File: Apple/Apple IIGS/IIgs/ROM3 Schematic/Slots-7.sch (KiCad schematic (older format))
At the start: 22 parts, among them J1 Apple_II_Slot, J2 Apple_II_Slot, J3 Apple_II_Slot, J4 Apple_II_Slot, J5 Apple_II_Slot, J6 Apple_II_Slot, J7 Apple_II_Slot

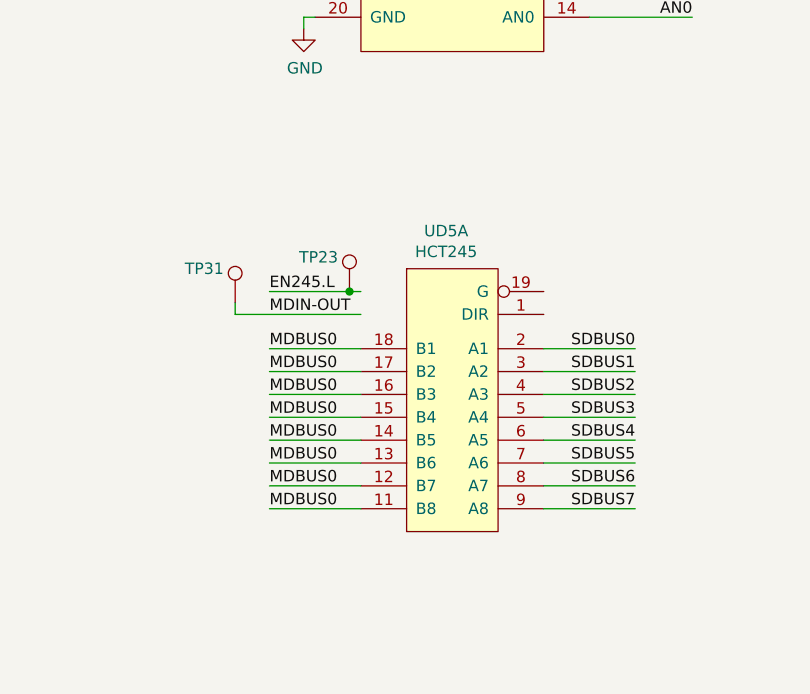
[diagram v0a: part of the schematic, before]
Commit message: Clean-up after detailed circuit analysis - Fixed Reference to library in project file - Fixed BABUS tags on HCT245 (had wrong nets) - Flipped HCT245 circuits on MEGAII page to better match In/Out flow - Changed HCT245 symbol to move enable and DIR to better match In/Out Flow - Changed HCT245 into multi-unit symbol to put VCC/GND pins on Unit B - Fixed MEGAII designator - Fixed ADBUS nets on HCT245 (should be ABUS!) - Added notes with lessons learned from circuit deep-dive
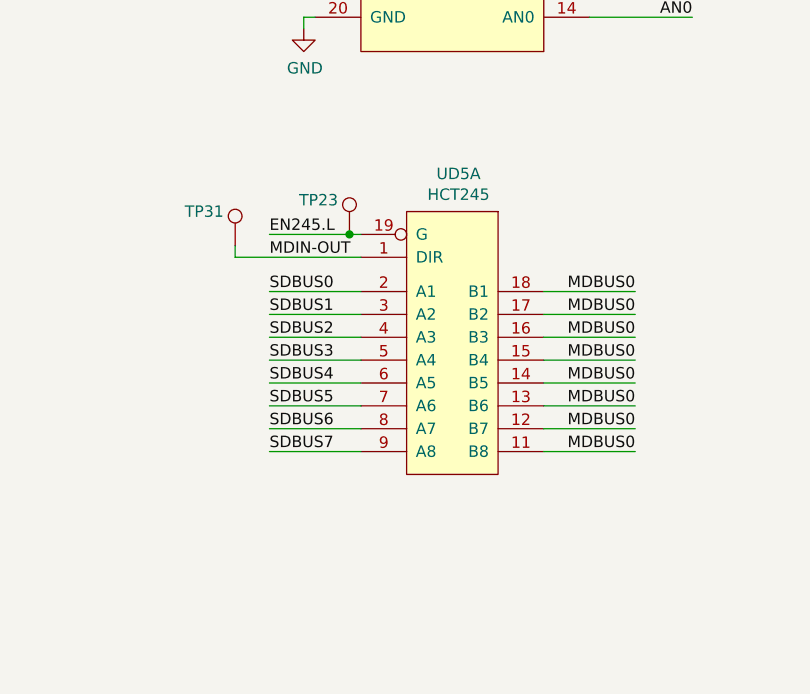
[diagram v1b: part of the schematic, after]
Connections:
- net EN245.L: now also UD5.19 (G)
- net MDIN-OUT: now also UD5.1 (DIR)
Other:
- moved on the sheet: TP23, TP31, UD5A
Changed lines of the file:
@@
-	1    0    0    -1
-$EndComp
-$Comp
-L IIgs-Schematic:HCT245 UD5
-U 1 1 5BF2195F
-P 2650 8500
-F 0 "UD5" H 2623 9265 50  0000 C CNN
-F 1 "HCT245" H 2623 9174 50  0000 C CNN
-F 2 "" H 2450 9150 50  0001 C CNN
-F 3 "" H 2450 9150 50  0001 C CNN
-	1    2650 8500
 	1    0    0    -1
 $EndComp
@@
 Wire Wire Line
 	2000 6800 2000 6850
-Wire Wire Line
-	3050 8250 3450 8250
-Text Label 3450 8250 2    50   ~ 0
-SDBUS0
-Wire Wire Line
-	3050 8350 3450 8350
-Text Label 3450 8350 2    50   ~ 0
-SDBUS1
-Wire Wire Line
-	3050 8450 3450 8450
-Text Label 3450 8450 2    50   ~ 0
-SDBUS2
-Wire Wire Line
-	3050 8550 3450 8550
-Text Label 3450 8550 2    50   ~ 0
-SDBUS3
-Wire Wire Line
-	3050 8650 3450 8650
-Text Label 3450 8650 2    50   ~ 0
-SDBUS4
-Wire Wire Line
-	3050 8750 3450 8750
-Text Label 3450 8750 2    50   ~ 0
-SDBUS5
-Wire Wire Line
-	3050 8850 3450 8850
-Text Label 3450 8850 2    50   ~ 0
-SDBUS6
-Wire Wire Line
-	3050 8950 3450 8950
-Text Label 3450 8950 2    50   ~ 0
-SDBUS7
-Text Label 1850 8250 0    50   ~ 0
+Text Label 3450 8000 2    50   ~ 0
 MDBUS0
-Text Label 1850 8350 0    50   ~ 0
+Text Label 3450 8100 2    50   ~ 0
 MDBUS0
-Text Label 1850 8450 0    50   ~ 0
+Text Label 3450 8200 2    50   ~ 0
 MDBUS0
-Text Label 1850 8550 0    50   ~ 0
+Text Label 3450 8300 2    50   ~ 0
 MDBUS0
-Text Label 1850 8650 0    50   ~ 0
+Text Label 3450 8400 2    50   ~ 0
 MDBUS0
-Text Label 1850 8750 0    50   ~ 0
+Text Label 3450 8500 2    50   ~ 0
 MDBUS0
-Text Label 1850 8850 0    50   ~ 0
+Text Label 3450 8600 2    50   ~ 0
 MDBUS0
-Text Label 1850 8950 0    50   ~ 0
+Text Label 3450 8700 2    50   ~ 0
 MDBUS0
-Wire Wire Line
-	1850 8850 2250 8850
-Wire Wire Line
-	2250 8750 1850 8750
-Wire Wire Line
-	1850 8650 2250 8650
-Wire Wire Line
-	2250 8550 1850 8550
-Wire Wire Line
-	1850 8450 2250 8450
-Wire Wire Line
-	1850 8350 2250 8350
-Wire Wire Line
-	2250 8250 1850 8250
-Text Label 1850 8100 0    50   ~ 0
+Text Label 1850 7850 0    50   ~ 0
 MDIN-OUT
 $Comp
 L Connector:TestPoint TP31
 U 1 1 5E2A0BC4
-P 1700 8050
-F 0 "TP31" H 1650 8200 50  0000 R CNN
-F 1 "TestPoint" H 1642 8168 50  0001 R CNN
-F 2 "" H 1900 8050 50  0001 C CNN
-F 3 "~" H 1900 8050 50  0001 C CNN
-	1    1700 8050
+P 1700 7800
+F 0 "TP31" H 1650 7950 50  0000 R CNN
+F 1 "TestPoint" H 1642 7918 50  0001 R CNN
+F 2 "" H 1900 7800 50  0001 C CNN
+F 3 "~" H 1900 7800 50  0001 C CNN
+	1    1700 7800
 	1    0    0    -1
 $EndComp
 Wire Wire Line
-	1700 8100 1700 8050
-Wire Wire Line
-	1700 8100 2250 8100
-Wire Wire Line
-	2250 8000 2200 8000
-Text Label 1850 8000 0    50   ~ 0
+	1700 7850 1700 7800
+Wire Wire Line
+	1700 7850 2250 7850
+Wire Wire Line
+	2250 7750 2200 7750
+Text Label 1850 7750 0    50   ~ 0
 EN245.L
 $Comp
 L Connector:TestPoint TP23
 U 1 1 5E36B3FB
-P 2200 8000
-F 0 "TP23" H 2150 8150 50  0000 R CNN
-F 1 "TestPoint" H 2142 8118 50  0001 R CNN
-F 2 "" H 2400 8000 50  0001 C CNN
-F 3 "~" H 2400 8000 50  0001 C CNN
-	1    2200 8000
+P 2200 7750
+F 0 "TP23" H 2150 7900 50  0000 R CNN
+F 1 "TestPoint" H 2142 7868 50  0001 R CNN
+F 2 "" H 2400 7750 50  0001 C CNN
+F 3 "~" H 2400 7750 50  0001 C CNN
+	1    2200 7750
 	1    0    0    -1
 $EndComp
-Connection ~ 2200 8000
-Wire Wire Line
-	2200 8000 1850 8000
-Wire Wire Line
-	1850 8950 2250 8950
+Connection ~ 2200 7750
+Wire Wire Line
+	2200 7750 1850 7750
 $Comp
 L Device:R_Small R113
@@
 Text Notes 2300 700  0    50   ~ 0
 Global labels not shown
+Wire Wire Line
+	3450 8700 3050 8700
+Wire Wire Line
+	3050 8000 3450 8000
+Wire Wire Line
+	3450 8100 3050 8100
+Wire Wire Line
+	3450 8200 3050 8200
+Wire Wire Line
+	3050 8300 3450 8300
+Wire Wire Line
+	3450 8400 3050 8400
+Wire Wire Line
+	3050 8500 3450 8500
+Wire Wire Line
+	3450 8600 3050 8600
+Text Label 1850 8700 0    50   ~ 0
+SDBUS7
+Wire Wire Line
+	2250 8700 1850 8700
+Text Label 1850 8600 0    50   ~ 0
+SDBUS6
+Wire Wire Line
+	2250 8600 1850 8600
+Text Label 1850 8500 0    50   ~ 0
+SDBUS5
+Wire Wire Line
+	2250 8500 1850 8500
+Text Label 1850 8400 0    50   ~ 0
+SDBUS4
+Wire Wire Line
+	2250 8400 1850 8400
+Text Label 1850 8300 0    50   ~ 0
+SDBUS3
+Wire Wire Line
+	2250 8300 1850 8300
+Text Label 1850 8200 0    50   ~ 0
+SDBUS2
+Wire Wire Line
+	2250 8200 1850 8200
+Text Label 1850 8100 0    50   ~ 0
+SDBUS1
+Wire Wire Line
+	2250 8100 1850 8100
+Text Label 1850 8000 0    50   ~ 0
+SDBUS0
+Wire Wire Line
+	2250 8000 1850 8000
+$Comp
+L IIgs-Schematic:HCT245 UD5
+U 1 1 5BF2195F
+P 2650 8250
+F 0 "UD5" H 2623 9015 50  0000 C CNN
+F 1 "HCT245" H 2623 8924 50  0000 C CNN
+F 2 "" H 2450 8900 50  0001 C CNN
+F 3 "" H 2450 8900 50  0001 C CNN
+	1    2650 8250
+	-1   0    0    -1
+$EndComp
 $EndSCHEMATC

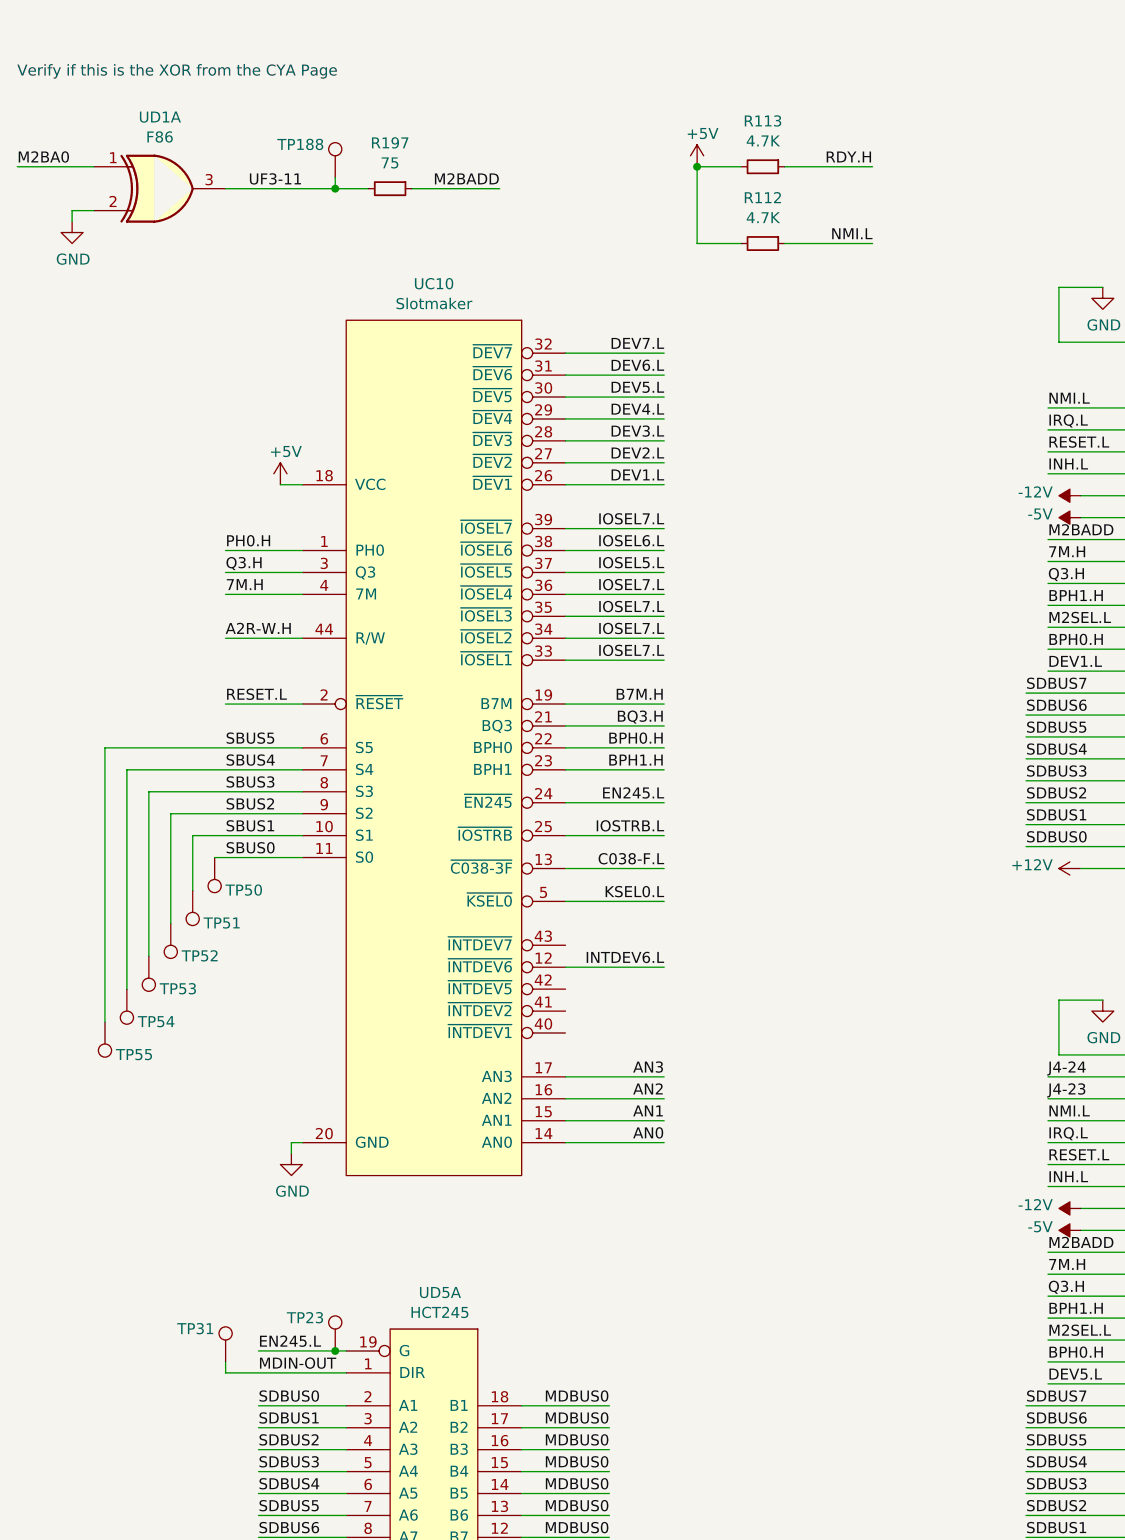
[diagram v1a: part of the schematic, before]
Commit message: started v2 updates on iigs-rom3
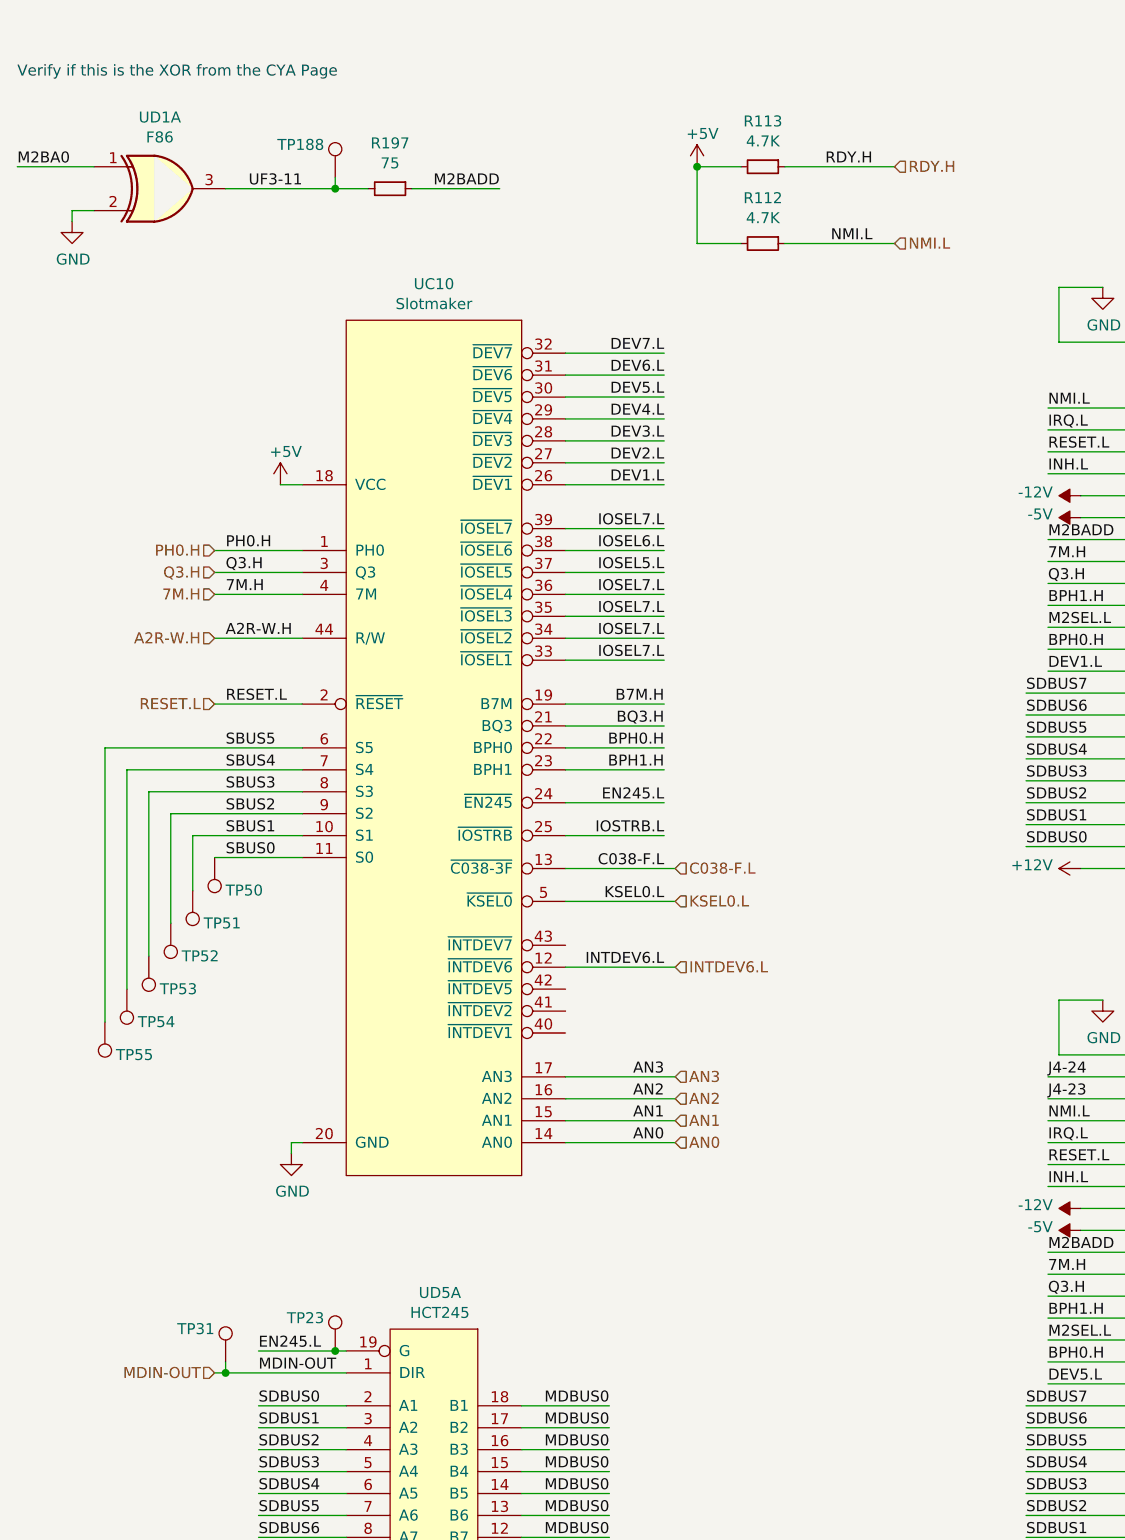
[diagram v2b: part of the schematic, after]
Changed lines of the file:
@@
 $Descr A3 16535 11693
 encoding utf-8
-Sheet 8 10
+Sheet 7 10
 Title ""
 Date ""
-Rev ""
+Rev "2"
 Comp ""
 Comment1 ""
@@
 Wire Wire Line
 	3250 5250 3700 5250
-Wire Wire Line
-	3250 6500 3700 6500
 Text Label 3700 6500 2    50   ~ 0
 AN3
-Wire Wire Line
-	3250 6600 3700 6600
 Text Label 3700 6600 2    50   ~ 0
 AN2
-Wire Wire Line
-	3250 6700 3700 6700
 Text Label 3700 6700 2    50   ~ 0
 AN1
-Wire Wire Line
-	3250 6800 3700 6800
 Text Label 3700 6800 2    50   ~ 0
 AN0
-Wire Wire Line
-	3250 6000 3700 6000
 Text Label 3700 6000 2    50   ~ 0
 INTDEV6.L
-Wire Wire Line
-	3250 5700 3700 5700
 Text Label 3700 5700 2    50   ~ 0
 KSEL0.L
-Wire Wire Line
-	3250 5550 3700 5550
 Text Label 3700 5550 2    50   ~ 0
 C038-F.L
@@
 Text Label 1700 4800 0    50   ~ 0
 RESET.L
-Wire Wire Line
-	1700 4800 2050 4800
-Wire Wire Line
-	2050 4500 1700 4500
 Text Label 1700 4500 0    50   ~ 0
 A2R-W.H
-Wire Wire Line
-	2050 4300 1700 4300
 Text Label 1700 4300 0    50   ~ 0
 7M.H
-Wire Wire Line
-	2050 4200 1700 4200
 Text Label 1700 4200 0    50   ~ 0
 Q3.H
-Wire Wire Line
-	2050 4100 1700 4100
 Text Label 1700 4100 0    50   ~ 0
 PH0.H
@@
 M2BADD
 Wire Wire Line
-	4250 2350 4650 2350
-Wire Wire Line
-	4250 2700 4650 2700
-Wire Wire Line
 	3850 2350 4050 2350
 Wire Wire Line
@@
 	-1   0    0    -1
 $EndComp
+Text HLabel 4750 2350 2    50   Input ~ 0
+RDY.H
+Text HLabel 4750 2700 2    50   Input ~ 0
+NMI.L
+Wire Wire Line
+	4250 2700 4750 2700
+Wire Wire Line
+	4250 2350 4750 2350
+Text HLabel 1650 4100 0    50   Input ~ 0
+PH0.H
+Text HLabel 1650 4200 0    50   Input ~ 0
+Q3.H
+Text HLabel 1650 4300 0    50   Input ~ 0
+7M.H
+Text HLabel 1650 4500 0    50   Input ~ 0
+A2R-W.H
+Wire Wire Line
+	1650 4100 2050 4100
+Wire Wire Line
+	1650 4200 2050 4200
+Wire Wire Line
+	1650 4300 2050 4300
+Wire Wire Line
+	1650 4500 2050 4500
+Text HLabel 1650 4800 0    50   Input ~ 0
+RESET.L
+Wire Wire Line
+	1650 4800 2050 4800
+Text HLabel 3750 5700 2    50   Input ~ 0
+KSEL0.L
+Wire Wire Line
+	3250 5700 3750 5700
+Text HLabel 3750 6500 2    50   Input ~ 0
+AN3
+Text HLabel 3750 6600 2    50   Input ~ 0
+AN2
+Text HLabel 3750 6700 2    50   Input ~ 0
+AN1
+Text HLabel 3750 6800 2    50   Input ~ 0
+AN0
+Wire Wire Line
+	3250 6800 3750 6800
+Wire Wire Line
+	3250 6700 3750 6700
+Wire Wire Line
+	3250 6600 3750 6600
+Wire Wire Line
+	3250 6500 3750 6500
+Text HLabel 3750 6000 2    50   Input ~ 0
+INTDEV6.L
+Wire Wire Line
+	3250 6000 3750 6000
+Text HLabel 3750 5550 2    50   Input ~ 0
+C038-F.L
+Wire Wire Line
+	3250 5550 3750 5550
+Text HLabel 1650 7850 0    50   Input ~ 0
+MDIN-OUT
+Wire Wire Line
+	1650 7850 1700 7850
+Connection ~ 1700 7850
 $EndSCHEMATC

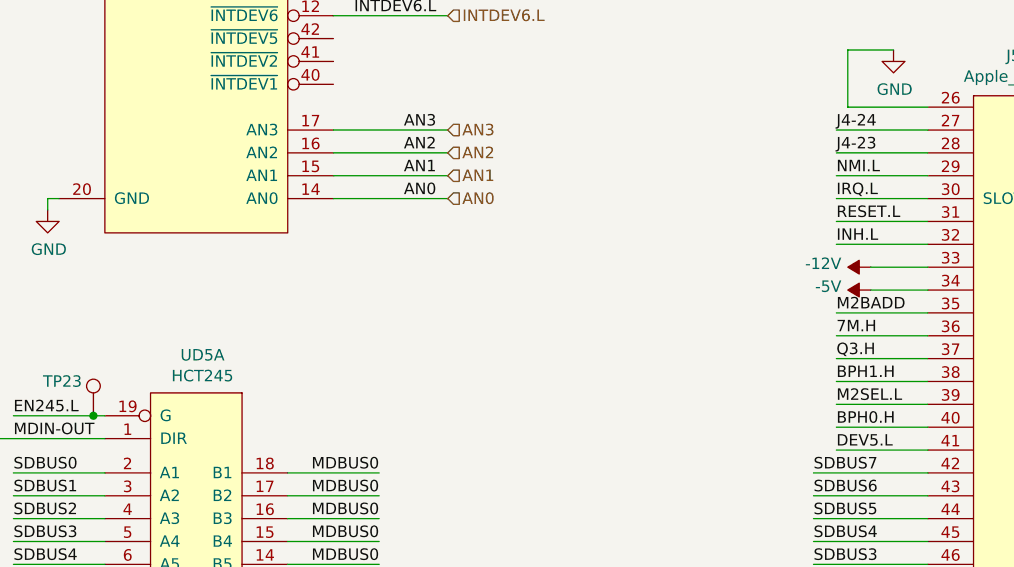
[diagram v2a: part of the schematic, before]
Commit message: added some notes, few rev2 changes, going to branch.
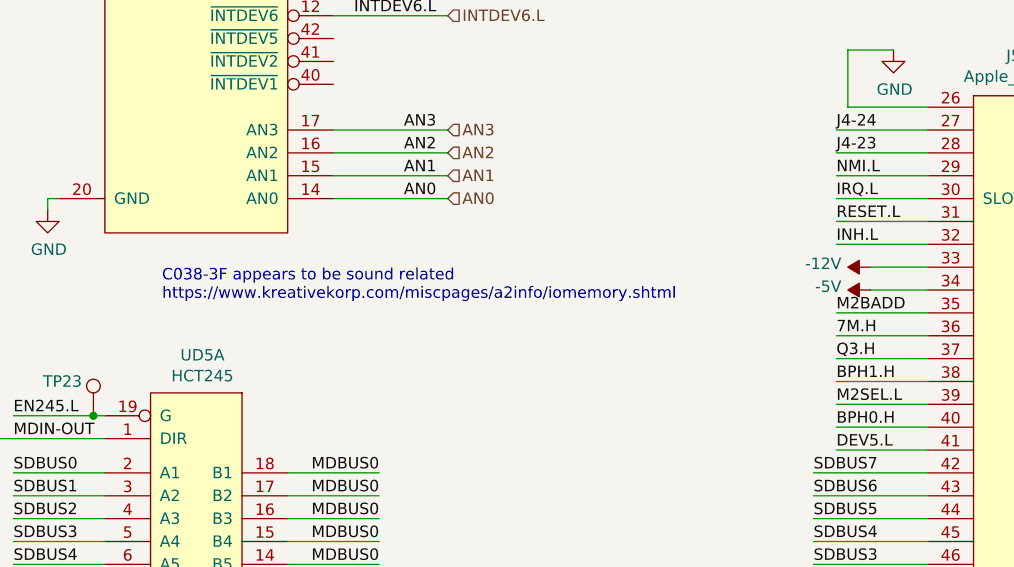
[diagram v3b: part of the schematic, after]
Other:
- note added: "C038-3F appears to be sound related\nhttps://www.kreativekorp.com/miscpages/a2info/iomemory.shtml"
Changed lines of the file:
@@
 	1650 7850 1700 7850
 Connection ~ 1700 7850
+Text Notes 2500 7250 0    50   ~ 0
+C038-3F appears to be sound related\nhttps://www.kreativekorp.com/miscpages/a2info/iomemory.shtml
 $EndSCHEMATC
